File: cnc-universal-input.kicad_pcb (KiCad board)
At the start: 2 copper layers, 96.5 x 96.5 mm, 124 parts, among them J1 3PT, J10 2PT, J11 8PT, J12 USB_B_Mini, J13 2PT, J14 2PT, J2 3PT, J3 3PT, J4 3PT, J5 3PT, J6 3PT, J7 3PT, J8 3PT, J9 AVR-ISP-6, Q1 2N7002, Q11 2N7002, Q12 2N7002, Q13 2N7002, SW1 RESET, SW2 BTN, U1 ATmega328PB-AU, U10 SFH617A-4, U11 SFH617A-4, U12 SFH617A-4, U13 SFH617A-4, U14 SFH617A-4, U15 SFH617A-4, U16 SFH617A-4, U18 CH340G, U19 TS2596S, U2 74HC595, U3 74HC595, U4 74HC595, U5 4051, U6 TS2596S, U8 LM7321, U9 SFH617A-4, Y1 18.432Mhz, Y2 12MHz

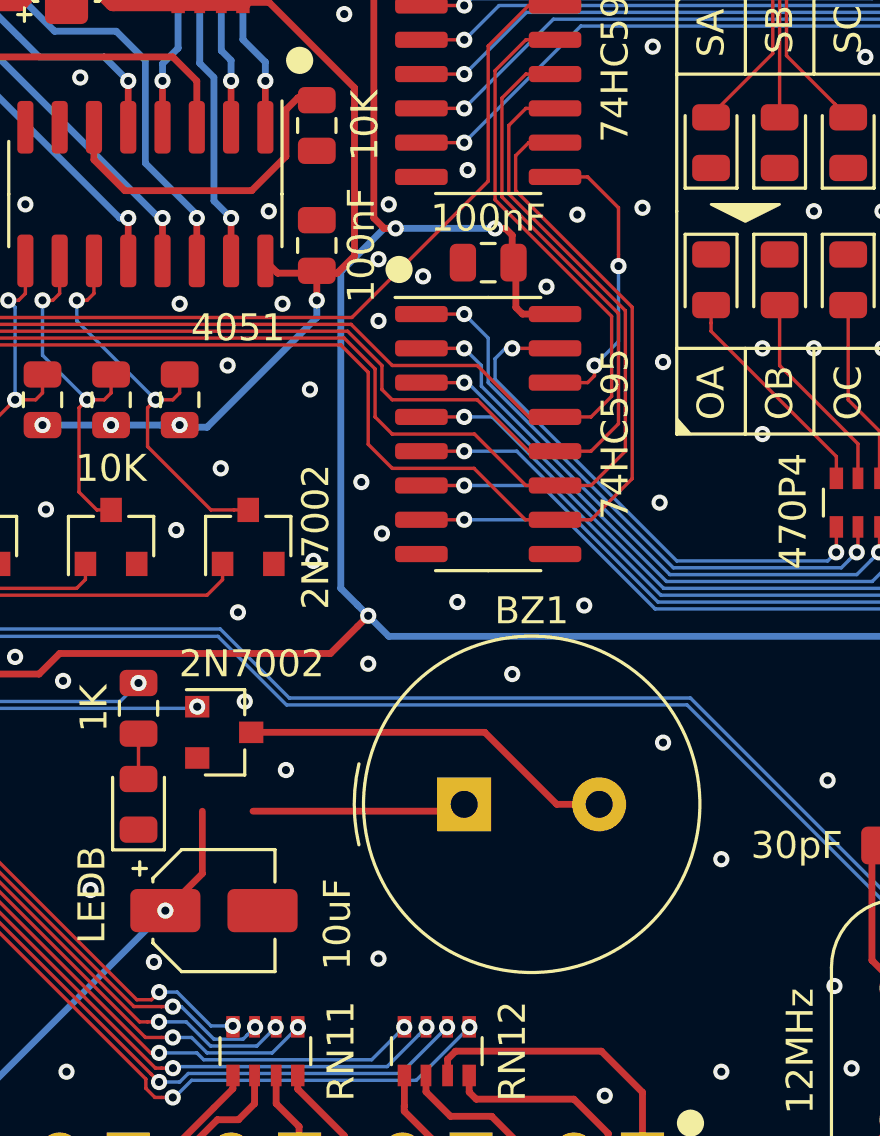
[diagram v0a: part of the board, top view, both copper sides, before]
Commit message: Changed Footprint
5mm rm buzzers don't exist
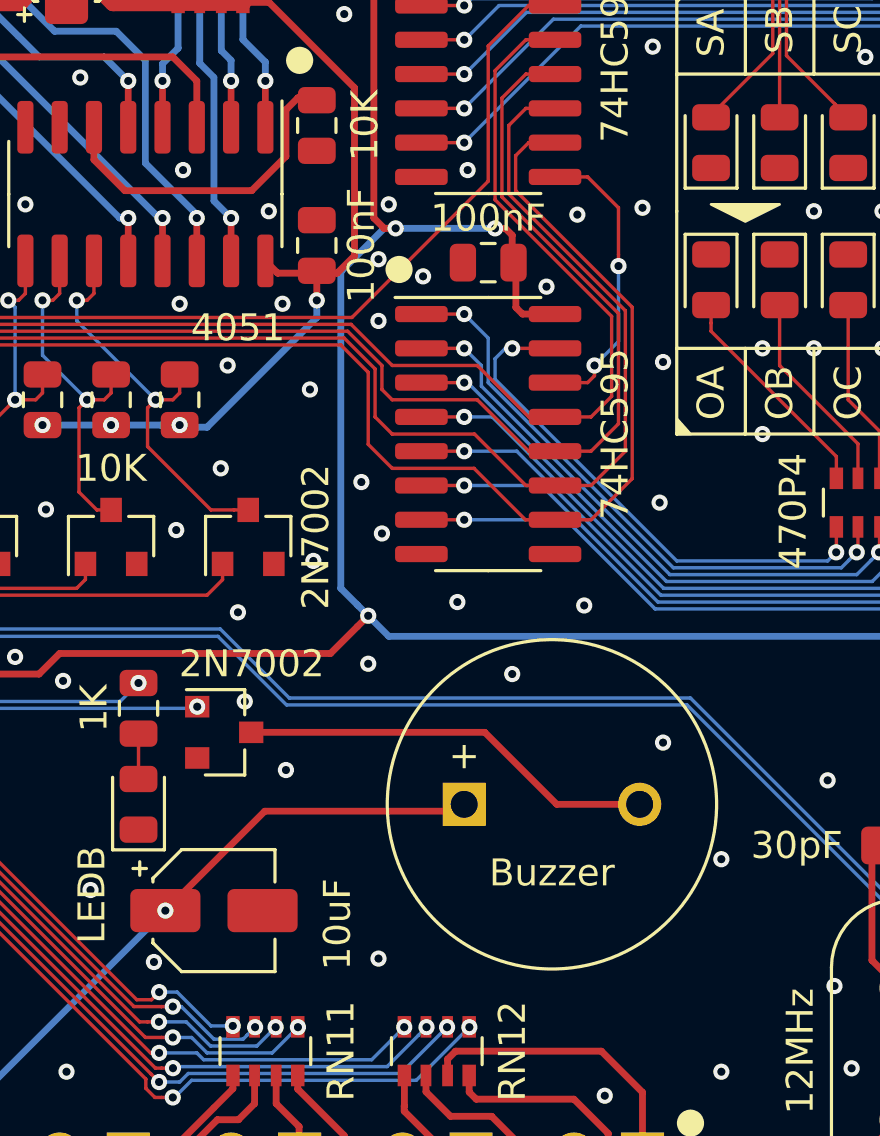
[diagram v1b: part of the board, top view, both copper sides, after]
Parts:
- BZ1: footprint Buzzer_Beeper:Buzzer_TDK_PS1240P02BT_D12.2mm_H6.5mm -> Buzzer_Beeper:MagneticBuzzer_ProSignal_ABT-410-RC
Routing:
- net Net-(BZ1-Pad2): track 14.0 -> 15.5 mm
- net +12V: track 346.9 -> 347.4 mm
- net GND: vias 302 -> 303
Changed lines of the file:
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@@
     (add_net "Net-(D8-Pad2)")
     (add_net "Net-(D9-Pad2)")
+    (add_net "Net-(J12-Pad1)")
     (add_net "Net-(J12-Pad2)")
     (add_net "Net-(J12-Pad3)")
+    (add_net "Net-(J12-Pad4)")
     (add_net "Net-(J12-Pad6)")
     (add_net "Net-(R34-Pad1)")
@@
     (add_net "Net-(RN6-Pad7)")
     (add_net "Net-(RN6-Pad8)")
+    (add_net "Net-(U1-Pad3)")
+    (add_net "Net-(U1-Pad6)")
+    (add_net "Net-(U18-Pad10)")
+    (add_net "Net-(U18-Pad11)")
+    (add_net "Net-(U18-Pad12)")
+    (add_net "Net-(U18-Pad13)")
+    (add_net "Net-(U18-Pad14)")
+    (add_net "Net-(U18-Pad15)")
+    (add_net "Net-(U18-Pad9)")
+    (add_net "Net-(U2-Pad9)")
+    (add_net "Net-(U3-Pad9)")
     (add_net "Net-(U5-Pad3)")
+    (add_net "Net-(U8-Pad1)")
+    (add_net "Net-(U8-Pad5)")
+    (add_net "Net-(U8-Pad8)")
+  )
+  (module Buzzer_Beeper:MagneticBuzzer_ProSignal_ABT-410-RC (layer F.Cu)
+    (at 231.521 -57.404)
+    (descr "Buzzer, Elektromagnetic Beeper, Summer, 1,5V-DC,")
+    (tags "Pro Signal ABT-410-RC ")
+    (fp_text reference BZ1 (at 3.25 -7) (layer F.SilkS) hide
+      (effects (font (size 1 1) (thickness 0.15)))
+    )
+    (fp_text value Buzzer (at 3.25 2.54) (layer F.SilkS)
+      (effects (font (size 1 1) (thickness 0.15)))
+    )
+    (fp_circle (center 3.25 0) (end 9.25 0) (layer F.Fab) (width 0.1))
+    (fp_circle (center 3.25 0) (end 4.4 0) (layer F.Fab) (width 0.1))
+    (fp_text user %R (at 3.25 -7) (layer F.Fab)
+      (effects (font (size 1 1) (thickness 0.15)))
+    )
+    (fp_text user + (at 0 -1.8) (layer F.SilkS)
+      (effects (font (size 1 1) (thickness 0.15)))
+    )
+    (fp_circle (center 3.25 0) (end 9.35 0) (layer F.SilkS) (width 0.12))
+    (fp_circle (center 3.25 0) (end 9.5 0) (layer F.CrtYd) (width 0.05))
+    (fp_text user + (at 0 -1.8) (layer F.Fab)
+      (effects (font (size 1 1) (thickness 0.15)))
+    )
+    (pad 2 thru_hole circle (at 6.5 0) (size 1.6 1.6) (drill 1) (layers *.Cu *.Mask)
+      (net 124 "Net-(BZ1-Pad2)"))
+    (pad 1 thru_hole rect (at 0 0) (size 1.6 1.6) (drill 1) (layers *.Cu *.Mask)
+      (net 5 +12V))
+    (model ${KISYS3DMOD}/Buzzer_Beeper.3dshapes/MagneticBuzzer_ProSignal_ABT-410-RC.wrl
+      (at (xyz 0 0 0))
+      (scale (xyz 1 1 1))
+      (rotate (xyz 0 0 0))
+    )
   )
   (module Package_QFP:TQFP-32_7x7mm_P0.8mm (layer F.Cu)
@@
     )
   )
-  (module Buzzer_Beeper:Buzzer_TDK_PS1240P02BT_D12.2mm_H6.5mm (layer F.Cu)
-    (at 231.521 -57.404)
-    (descr "Buzzer, D12.2mm height 6.5mm, https://product.tdk.com/info/en/catalog/datasheets/piezoelectronic_buzzer_ps_en.pdf")
-    (tags buzzer)
-    (fp_text reference BZ1 (at 2.5 -7.17) (layer F.SilkS)
-      (effects (font (size 1 1) (thickness 0.15)))
-    )
-    (fp_text value Buzzer (at 2.5 7.31) (layer F.Fab)
-      (effects (font (size 1 1) (thickness 0.15)))
-    )
-    (fp_line (start -1.3 -1) (end -1.3 1) (layer F.Fab) (width 0.1))
-    (fp_circle (center 2.5 0) (end 8.73 0) (layer F.SilkS) (width 0.12))
-    (fp_circle (center 2.5 0) (end 3.5 0) (layer F.Fab) (width 0.1))
-    (fp_circle (center 2.5 0) (end 8.6 0) (layer F.Fab) (width 0.1))
-    (fp_circle (center 2.5 0) (end 8.85 0) (layer F.CrtYd) (width 0.05))
-    (fp_arc (start 2.5 0) (end -3.9 -1.5) (angle -26.38121493) (layer F.SilkS) (width 0.12))
-    (fp_text user %R (at 2.5 -2.43) (layer F.Fab)
-      (effects (font (size 1 1) (thickness 0.15)))
-    )
-    (pad 2 thru_hole circle (at 5 0) (size 2 2) (drill 1) (layers *.Cu *.Mask)
-      (net 124 "Net-(BZ1-Pad2)"))
-    (pad 1 thru_hole rect (at 0 0) (size 2 2) (drill 1) (layers *.Cu *.Mask)
-      (net 5 +12V))
-    (model ${KISYS3DMOD}/Buzzer_Beeper.3dshapes/Buzzer_TDK_PS1240P02BT_D12.2mm_H6.5mm.wrl
-      (at (xyz 0 0 0))
-      (scale (xyz 1 1 1))
-      (rotate (xyz 0 0 0))
-    )
-  )
   (module Package_DIP:DIP-4_W7.62mm (layer F.Cu)
     (at 238.125 -33.655 270)
@@
   (via (at 227.076 -86.6775) (size 0.6) (drill 0.3) (layers F.Cu B.Cu) (net 2))
   (via (at 209.423 -67.945) (size 0.6) (drill 0.3) (layers F.Cu B.Cu) (net 2))
+  (via (at 221.107 -80.899) (size 0.6) (drill 0.3) (layers F.Cu B.Cu) (net 2))
   (segment (start 190.509 -65.215) (end 190.509 -61.341) (width 0.127) (layer F.Cu) (net 3))
   (segment (start 189.484 -66.24) (end 190.509 -65.215) (width 0.127) (layer F.Cu) (net 3))
@@
   (segment (start 213.46501 -46.482) (end 220.45 -53.46699) (width 0.25) (layer B.Cu) (net 5))
   (segment (start 199.9765 -46.482) (end 213.46501 -46.482) (width 0.25) (layer B.Cu) (net 5))
-  (segment (start 221.8205 -54.8375) (end 220.45 -53.467) (width 0.25) (layer F.Cu) (net 5))
-  (segment (start 221.8205 -57.15) (end 221.8205 -54.8375) (width 0.25) (layer F.Cu) (net 5))
   (via (at 207.9 -87.95) (size 0.6) (drill 0.3) (layers F.Cu B.Cu) (net 5))
   (via (at 208.769501 -87.069499) (size 0.6) (drill 0.3) (layers F.Cu B.Cu) (net 5))
@@
   (segment (start 192.786 -46.482) (end 192.024 -45.72) (width 0.635) (layer F.Cu) (net 5))
   (segment (start 231.267 -57.15) (end 231.521 -57.404) (width 0.25) (layer F.Cu) (net 5))
-  (segment (start 223.6955 -57.15) (end 231.267 -57.15) (width 0.25) (layer F.Cu) (net 5))
+  (segment (start 220.45 -53.467) (end 224.133 -57.15) (width 0.25) (layer F.Cu) (net 5))
+  (segment (start 224.133 -57.15) (end 231.267 -57.15) (width 0.25) (layer F.Cu) (net 5))
   (via (at 260.604 -55.88) (size 0.6) (drill 0.3) (layers F.Cu B.Cu) (net 6))
   (via (at 194.437 -88.519) (size 0.6) (drill 0.3) (layers F.Cu B.Cu) (net 6))
@@
   (segment (start 235.585 -46.482) (end 236.855 -45.212) (width 0.254) (layer F.Cu) (net 123))
   (segment (start 236.855 -45.212) (end 236.855 -40.64) (width 0.254) (layer F.Cu) (net 123))
-  (segment (start 234.95 -57.404) (end 236.521 -57.404) (width 0.25) (layer F.Cu) (net 124))
   (segment (start 223.631 -60.071) (end 232.283 -60.071) (width 0.25) (layer F.Cu) (net 124))
+  (segment (start 234.95 -57.404) (end 238.021 -57.404) (width 0.25) (layer F.Cu) (net 124))
   (segment (start 232.283 -60.071) (end 234.95 -57.404) (width 0.25) (layer F.Cu) (net 124))
   (segment (start 201.74299 -65.811583) (end 201.802813 -65.811583) (width 0.127) (layer F.Cu) (net 125))

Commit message: Yeetus deletus
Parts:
- removed R64: 1K, Resistor_SMD:R_0805_2012Metric
- removed R65: 10K, Resistor_SMD:R_0805_2012Metric
- added C29: 100nF, Capacitor_SMD:C_0805_2012Metric, F.Cu at (208.2, -71.6)
- Y1: value 18.432Mhz -> 18.432MHz; footprint Crystal:Crystal_HC49-4H_Vertical -> Crystal:Crystal_SMD_EuroQuartz_MJ-4Pin_5.0x3.2mm
- moved C1 13.7 mm to (189.9, -62.1), turned to 180 degrees
- moved C2 9.16 mm to (190.0, -70.5), turned to 180 degrees
- moved Y1 4.85 mm to (190.0, -66.3)
- moved C19 1.54 mm to (194.2, -66.3)
- moved C9 0.74 mm to (205.5, -74.3)
- moved C17 0.63 mm to (199.4, -58.0)
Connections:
- C1 pad 1: GND -> Net-(C1-Pad1)
- C1 pad 2: Net-(C1-Pad2) -> GND
- SW2 pad 2: Net-(R64-Pad1) -> Net-(SW2-Pad2)
- U1 pad 28: Net-(R64-Pad2) -> Net-(SW2-Pad2)
- U1 pad 7: Net-(C1-Pad2) -> Net-(C2-Pad2)
- U1 pad 8: Net-(C2-Pad2) -> Net-(C1-Pad1)
- Y1 pad 1: Net-(C1-Pad2) -> Net-(C2-Pad2)
- Y1 pad 2: Net-(C2-Pad2) -> GND
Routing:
- net Net-(SW2-Pad2): track 0.00 -> 27.1 mm, vias 0 -> 4
- net Net-(R64-Pad2): track 21.8 -> 0.00 mm, vias 2 -> 0
- net Net-(C1-Pad2): track 21.1 -> 0.00 mm
- net Net-(C1-Pad1): track 0.00 -> 15.1 mm
- net Net-(R64-Pad1): track 12.2 -> 0.00 mm, vias 2 -> 0
- net Net-(C2-Pad2): track 17.6 -> 15.4 mm
- net GND: track 3.20 -> 2.33 mm, vias 303 -> 297
- net +5V: track 281.5 -> 282.2 mm

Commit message: Board stuff
Flipped the input polarity
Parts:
- C1, C2: value 30pF -> 22pF
- Y1: value 18.432MHz -> 16MHz
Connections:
- J10 pad 1: GND -> +24V
- J10 pad 2: +24V -> GND
- J13 pad 1: GNDD -> +5VD
- J13 pad 2: +5VD -> GNDD
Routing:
- net +24V: track 170.1 -> 164.7 mm
- net GNDD: track 88.8 -> 94.1 mm
- net +5VD: track 37.3 -> 38.1 mm
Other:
- board text added: "BAUD 38400"
- board text added: "GND"
- board text removed: "BAUD 115200"
